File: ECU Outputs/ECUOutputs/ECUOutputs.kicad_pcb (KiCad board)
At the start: 2 copper layers, 63 parts, among them J4 ECU CONNECTOR, Q1 BC817-40-TP, Q2 BC817-40-TP, Q3 BC817-40-TP, Q4 BC817-40-TP, Q5 BC817-40-TP, Q6 BC817-40-TP, Q7 BC817-40-TP, Q8 BC817-40-TP

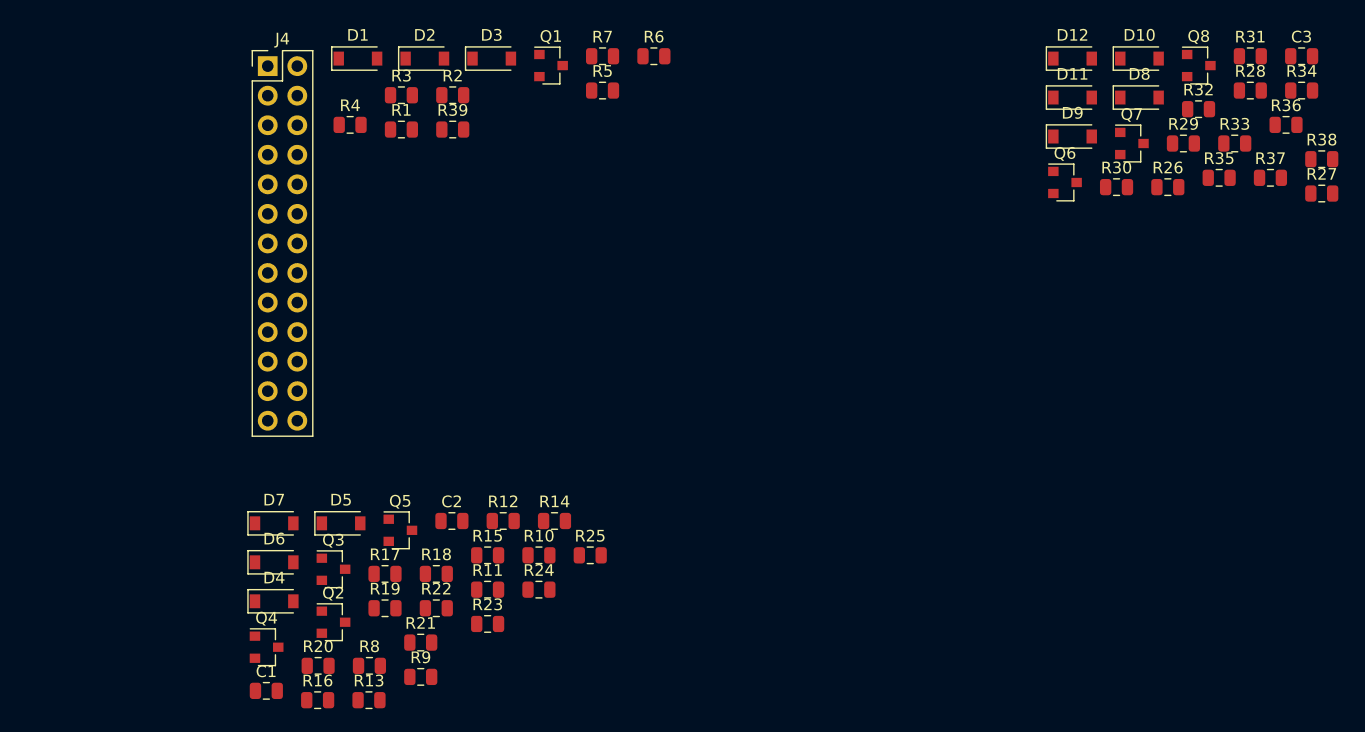
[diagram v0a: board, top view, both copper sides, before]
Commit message: Laid out ECU outputs PCB. Generated manufacturing files.
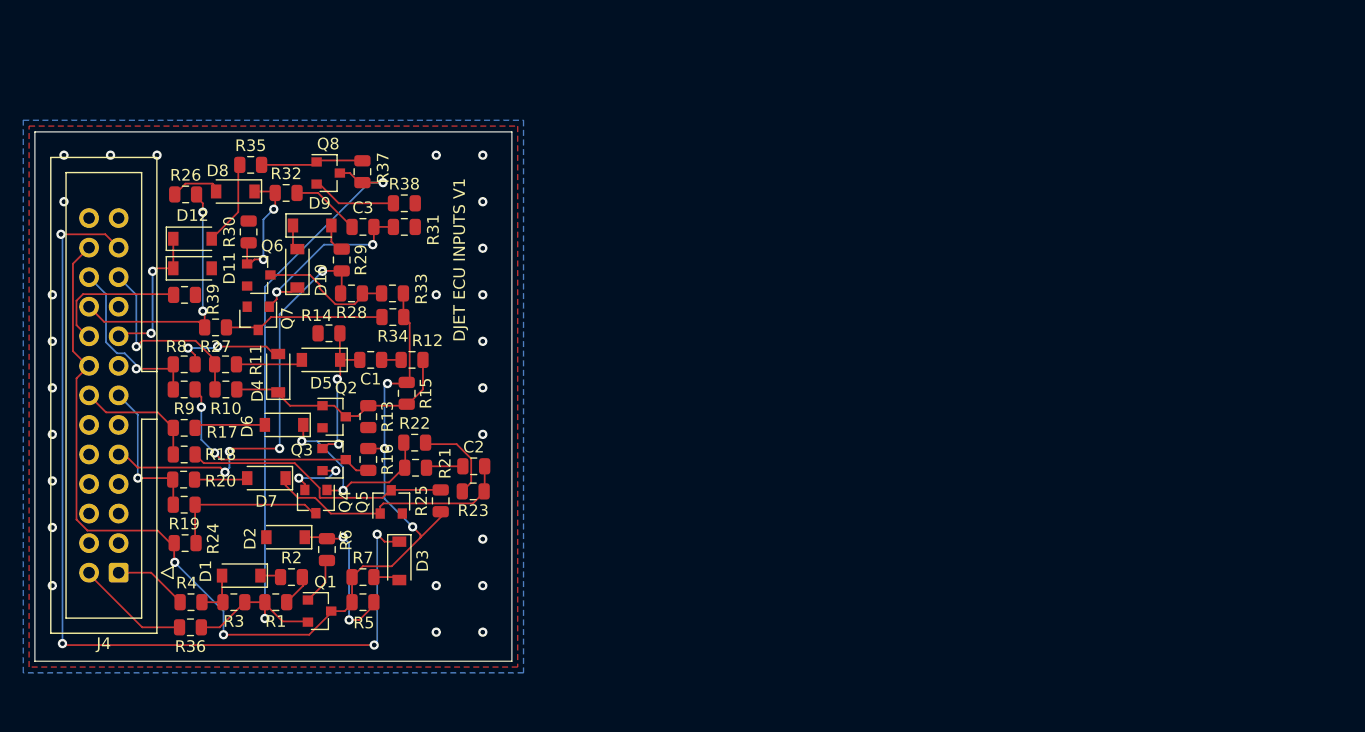
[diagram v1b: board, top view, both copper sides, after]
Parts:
- J4: footprint Connector_PinHeader_2.54mm:PinHeader_2x13_P2.54mm_Vertical -> Connector_IDC:IDC-Header_2x13_P2.54mm_Vertical
- moved R36 103.6 mm to (113.9, 108.6), turned to 180 degrees
- moved R27 95.8 mm to (116.0, 82.8), turned to 180 degrees
- moved R26 84.4 mm to (113.5, 71.4)
- moved R35 83.3 mm to (119.0, 68.8)
- moved C3 82.0 mm to (128.7, 74.2)
- moved R34 80.5 mm to (131.3, 81.9), turned to 180 degrees
- moved R28 79.2 mm to (127.7, 79.9), turned to 180 degrees
- moved R38 79.0 mm to (132.3, 72.1)
- moved R32 78.8 mm to (122.1, 71.2)
- moved D8 78.1 mm to (117.7, 71.1), turned to 180 degrees
- moved R37 78.1 mm to (128.7, 69.4), turned to 90 degrees
- moved D12 77.2 mm to (114.0, 75.2)
- moved D11 77.1 mm to (114.0, 77.7)
- moved Q7 76.6 mm to (119.7, 82.0), turned to 270 degrees
- moved Q8 75.4 mm to (125.7, 69.5)
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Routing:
- net +12V: track 0.00 -> 94.1 mm, vias 0 -> 5
- net /ECU_COOLANTTEMP: track 0.00 -> 79.1 mm, vias 0 -> 4
- net +10V: track 0.00 -> 58.5 mm, vias 0 -> 2
- net /ECU_TPSACCEL1: track 0.00 -> 36.0 mm, vias 0 -> 4
- net Net-(Q5-Pad3): track 0.00 -> 23.5 mm
- net Net-(C2-Pad2): track 0.00 -> 21.6 mm
- net /ECU_TPSACCEL2: track 0.00 -> 21.6 mm, vias 0 -> 2
- net Net-(D4-Pad1): track 0.00 -> 20.2 mm
- net Net-(Q3-Pad3): track 0.00 -> 19.6 mm, vias 0 -> 2
- net Net-(D6-Pad1): track 0.00 -> 17.3 mm, vias 0 -> 2
- net /ECU_TRIGGERGROUP1: track 0.00 -> 16.7 mm, vias 0 -> 1
- net Net-(C3-Pad2): track 0.00 -> 16.6 mm, vias 0 -> 2
- net /ECU_TRIGGERGROUP3: track 0.00 -> 15.1 mm, vias 0 -> 1
- net Net-(Q7-Pad3): track 0.00 -> 13.8 mm
- net Net-(Q4-Pad3): track 0.00 -> 13.7 mm
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- added copper zone on B.Cu, net GND
- added copper zone on F.Cu, net GND
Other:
- board outline added: 41 x 45.5 mm
- net class Default: clearance 0.2 -> 0.1524; trace_width 0.25 -> 0.1524
- rule trace_clearance: 0.2 -> 0.1524
- rule trace_min: 0.2 -> 0.1524
- board text added: "DJET ECU INPUTS V1"
